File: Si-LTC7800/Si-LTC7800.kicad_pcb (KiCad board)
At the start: 2 copper layers, 54.8 x 47.8 mm, 40 parts, among them Q1 BSC100N06LS3_G, Q2 BSC100N06LS3_G, U1 LTC7800HUDC_PBF

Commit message: Updating PCBs for preassembly
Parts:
- added RLOAD2: 2Ohm, Resistor_SMD:R_0201_0603Metric, F.Cu at (152.7, 125.8)
- C1, C2, C3, C5, C6, COUT1, CSENSE1, CinA1, CinA2: footprint Capacitor_SMD:C_0805_2012Metric_Pad1.18x1.45mm_HandSolder -> Capacitor_SMD:C_0805_2012Metric
- CinB1: footprint Capacitor_SMD:C_0805_2012Metric_Pad1.18x1.45mm_HandSolder -> Capacitor_Tantalum_SMD:CP_EIA-7343-31_Kemet-D
- R1, R2, R4, R5, R6, R7, R9, RSENSE1: footprint Resistor_SMD:R_0201_0603Metric_Pad0.64x0.40mm_HandSolder -> Resistor_SMD:R_0201_0603Metric
- RLOAD1: value 5Ohm -> 3Ohm; footprint Resistor_SMD:R_0201_0603Metric_Pad0.64x0.40mm_HandSolder -> Resistor_SMD:R_0201_0603Metric
- moved RLOAD1 6.03 mm to (154.0, 127.2), turned to 135 degrees
- moved CinB1 3.13 mm to (144.1, 155.7), turned to 0 degrees
- moved CinA1 0.45 mm to (138.6, 156.1)
- moved CinA1_EX1 0.44 mm to (134.6, 156.0)
- moved CinA2 0.44 mm to (136.6, 156.1)
- moved CinB1_EX1 0.44 mm to (132.6, 156.0)
- moved TP_VIN1 0.40 mm to (129.8, 153.5)
- moved VSource_IN1 0.07 mm to (137.0, 147.9)
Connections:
- RLOAD1 pad 2: GND -> Net-(RLOAD1-Pad2)
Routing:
- net /VIN: track 15.9 -> 27.1 mm
- net Net-(RLOAD1-Pad2): track 0.00 -> 1.31 mm

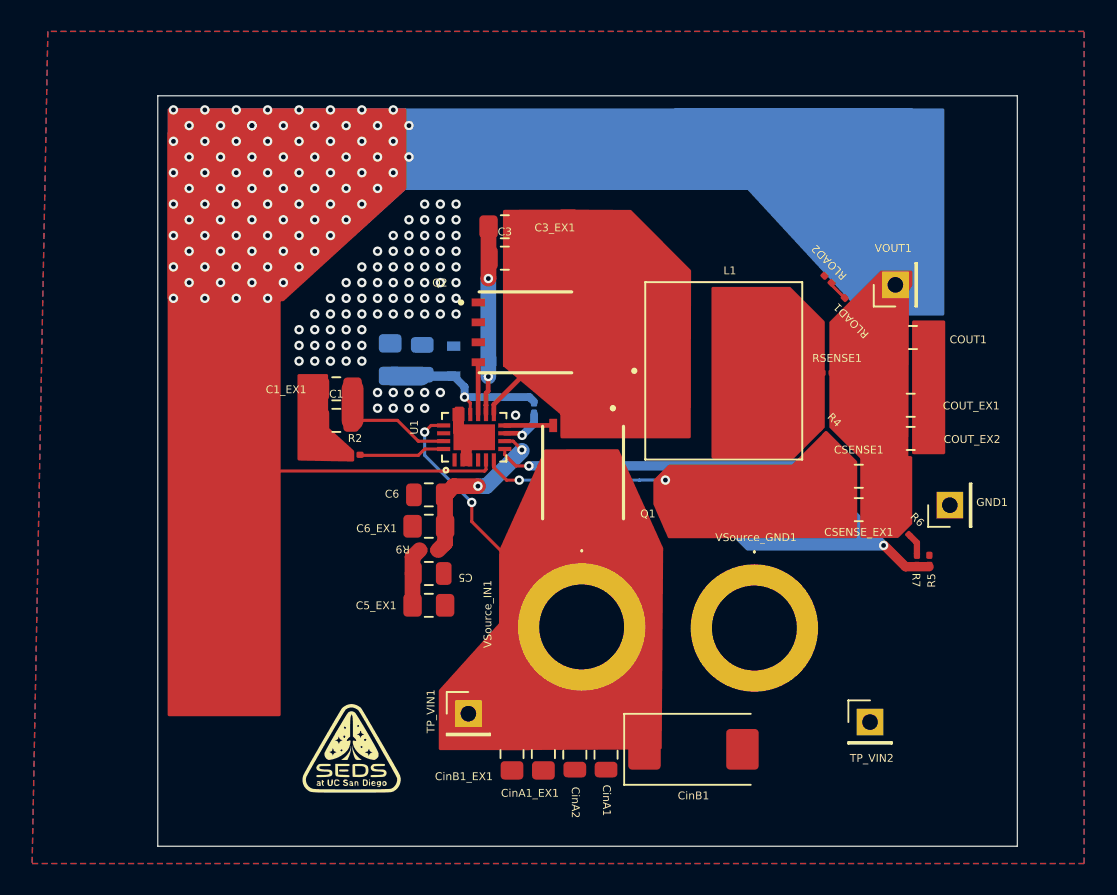
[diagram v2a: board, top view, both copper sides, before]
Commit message: mounting holes
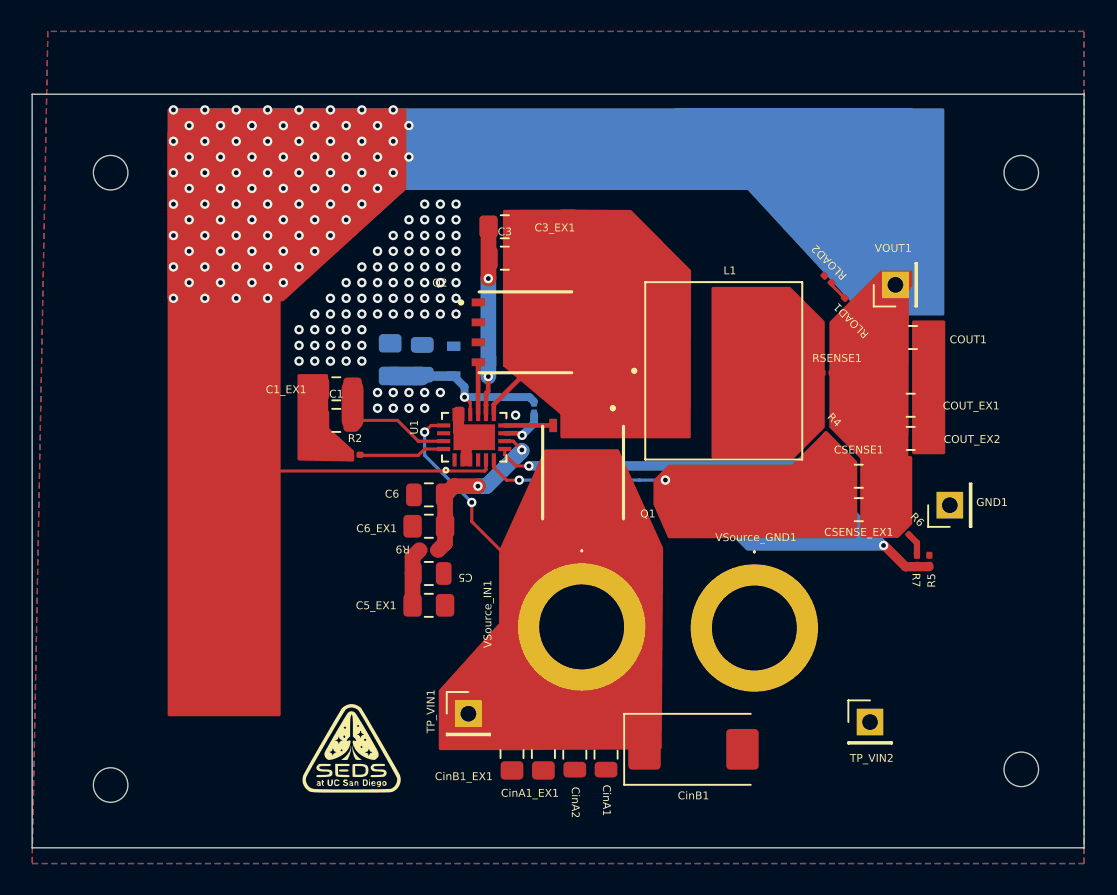
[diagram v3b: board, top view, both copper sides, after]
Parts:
- added REF**: MountingHole_2.2mm_M2, MountingHole:MountingHole_2.2mm_M2, F.Cu at (107.0, 119.0)
- added REF**: MountingHole_2.2mm_M2, MountingHole:MountingHole_2.2mm_M2, F.Cu at (165.0, 119.0)
- added REF**: MountingHole_2.2mm_M2, MountingHole:MountingHole_2.2mm_M2, F.Cu at (165.0, 157.0)
- added REF**: MountingHole_2.2mm_M2, MountingHole:MountingHole_2.2mm_M2, F.Cu at (107.0, 158.0)
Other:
- board size 54.8 x 47.8 mm -> 67 x 48 mm

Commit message: minor edits
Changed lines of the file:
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@@
 		(polygon
 			(pts
-				(xy 103 110) (xy 102 163) (xy 169 163) (xy 169 110)
+				(xy 101.952764 113.999724) (xy 101.998957 161.918043) (xy 169.002664 161.918043) (xy 169.120672 113.999724)
 			)
 		)
